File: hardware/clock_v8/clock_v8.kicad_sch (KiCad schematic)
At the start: 143 parts, among them J1 RJ45, J12 Conn_01x06, J2 Conn_01x06_Pin, J4 USB_C_Receptacle, J5 Conn_01x06_Pin, J6 Conn_01x04_Pin, J8 Conn_01x02, Q1 2N7002, Q10 2N7002, Q9 2N7002, U1 ADA4807-1, U10 STM32F405RGTx, U11 AMS1117-3.3, U12 BA50DD0WHFP-TR, U13 M24C02-RMN, U14 CH340C, U15 USBLC6-2P6, U2 SN74LVC1G14DBV, U3 SN74LVC1G14DBV, U4 ADA4807-1, U5 ADA4807-1, U6 TLV3603DCKR, U7 SN74LVC1G14DBV, U8 TLV3603DCKR, U9 L78L05_SOT89, Y1 AOCJY4A-10.000MHZ-SW, Y2 16MHz

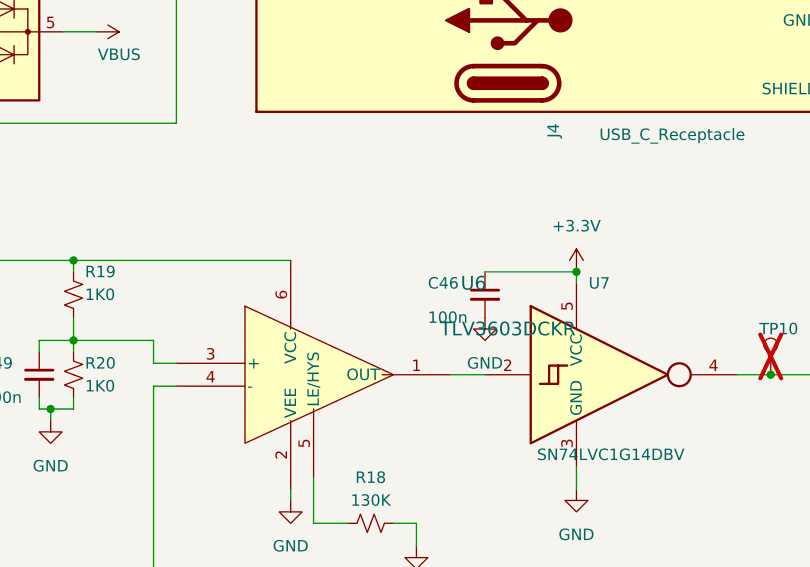
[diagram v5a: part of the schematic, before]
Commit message: move symbols and footprints to shared level
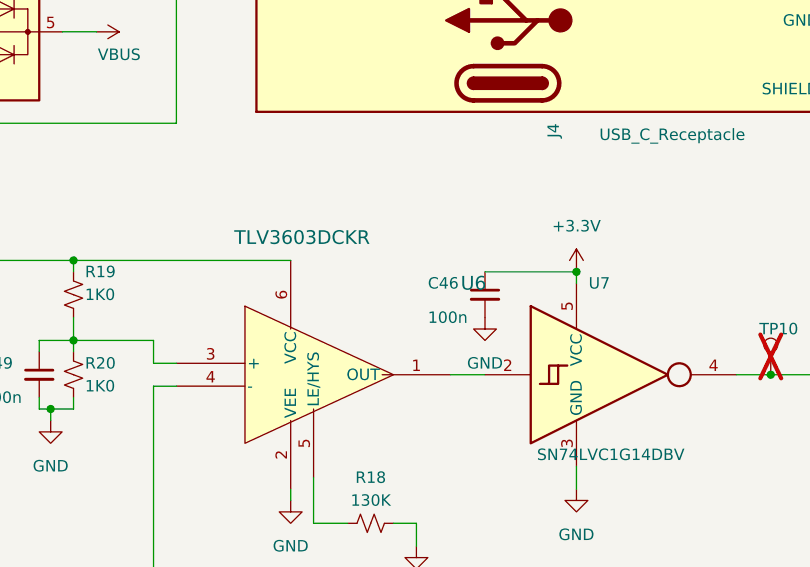
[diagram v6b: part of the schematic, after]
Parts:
- J4: symbol blinky:USB_C_Receptacle -> BlinkyShared:USB_C_Receptacle
- S1, S2, S3: symbol blinky:147873-2 -> BlinkyShared:147873-2
- U12: footprint blinky_footprints:DPAK172P1054X200-6N -> DPAK172P1054X200-6N; symbol blinky:BA50DD0WHFP-TR -> BlinkyShared:BA50DD0WHFP-TR; MAXIMUM_PACKAGE_HEIGHT (none) -> 2.005 mm; PARTREV (none) -> 003; STANDARD (none) -> IPC 7351B
- U6, U8: symbol blinky:TLV3603DCKR -> BlinkyShared:TLV3603DCKR
- Y1: footprint blinky_footprints:XTAL_AOCJY4A-10.000MHZ-SW -> XTAL_AOCJY4A-10.000MHZ-SW; symbol blinky:AOCJY4A-10.000MHZ-SW -> BlinkyShared:AOCJY4A-10.000MHZ-SW; MAXIMUM_PACKAGE_HEIGHT (none) -> 13.76 mm; PARTREV (none) -> 07.24.11; SNAPEDA_PN (none) -> AOCJY4A-10.000MHZ-SW; STANDARD (none) -> IPC_7351B; now in the parts list
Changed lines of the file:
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@@
   (junction (at 391.16 214.63) (diameter 0) (color 0 0 0 0)
   )
-  (junction (at 283.21 237.49) (diameter 0) (color 0 0 0 0)
-  )
   (junction (at 49.53 60.96) (diameter 0) (color 0 0 0 0)
   )
@@
   (junction (at 364.49 214.63) (diameter 0) (color 0 0 0 0)
   )
+  (junction (at 283.21 237.49) (diameter 0) (color 0 0 0 0)
+  )
   (junction (at 20.32 53.34) (diameter 0) (color 0 0 0 0)
   )
@@
     (stroke (width 0) (type default))
   )
-  (wire (pts (xy 283.21 237.49) (xy 283.21 241.3))
-    (stroke (width 0) (type default))
-  )
   (wire (pts (xy 229.87 252.73) (xy 236.22 252.73))
     (stroke (width 0) (type default))
@@
     (stroke (width 0) (type default))
   )
+  (wire (pts (xy 283.21 237.49) (xy 283.21 241.3))
+    (stroke (width 0) (type default))
+  )
   (wire (pts (xy 364.49 138.43) (xy 377.19 138.43))
     (stroke (width 0) (type default))
@@
     )
   )
-  (symbol (lib_id "blinky:AOCJY4A-10.000MHZ-SW") (at 252.73 160.02 0) (unit 1)
-    (in_bom no) (on_board yes) (dnp yes) (fields_autoplaced)
+  (symbol (lib_id "BlinkyShared:AOCJY4A-10.000MHZ-SW") (at 252.73 160.02 0) (unit 1)
+    (in_bom yes) (on_board yes) (dnp yes) (fields_autoplaced)
     (property "Reference" "Y1" (at 252.73 144.78 0)
       (effects (font (size 1.27 1.27)))
@@
       (effects (font (size 1.27 1.27)))
     )
-    (property "Footprint" "blinky_footprints:XTAL_AOCJY4A-10.000MHZ-SW" (at 252.73 160.02 0)
+    (property "Footprint" "XTAL_AOCJY4A-10.000MHZ-SW" (at 252.73 160.02 0)
       (effects (font (size 1.27 1.27)) (justify bottom) hide)
     )
@@
       (effects (font (size 1.27 1.27)) hide)
     )
-    (property "PARTREV" "" (at 252.73 160.02 0)
+    (property "PARTREV" "07.24.11" (at 252.73 160.02 0)
       (effects (font (size 1.27 1.27)) (justify bottom) hide)
     )
-    (property "STANDARD" "" (at 252.73 160.02 0)
+    (property "STANDARD" "IPC_7351B" (at 252.73 160.02 0)
       (effects (font (size 1.27 1.27)) (justify bottom) hide)
     )
-    (property "SNAPEDA_PN" "" (at 252.73 160.02 0)
+    (property "SNAPEDA_PN" "AOCJY4A-10.000MHZ-SW" (at 252.73 160.02 0)
       (effects (font (size 1.27 1.27)) (justify bottom) hide)
     )
-    (property "MAXIMUM_PACKAGE_HEIGHT" "" (at 252.73 160.02 0)
+    (property "MAXIMUM_PACKAGE_HEIGHT" "13.76 mm" (at 252.73 160.02 0)
       (effects (font (size 1.27 1.27)) (justify bottom) hide)
     )
@@
     )
   )
-  (symbol (lib_id "blinky:BA50DD0WHFP-TR") (at 46.99 171.45 0) (unit 1)
+  (symbol (lib_id "BlinkyShared:BA50DD0WHFP-TR") (at 46.99 171.45 0) (unit 1)
     (in_bom yes) (on_board yes) (dnp no) (fields_autoplaced)
     (property "Reference" "U12" (at 46.99 158.75 0)
@@
       (effects (font (size 1.27 1.27)))
     )
-    (property "Footprint" "blinky_footprints:DPAK172P1054X200-6N" (at 46.99 171.45 0)
+    (property "Footprint" "DPAK172P1054X200-6N" (at 46.99 171.45 0)
       (effects (font (size 1.27 1.27)) (justify bottom) hide)
     )
@@
       (effects (font (size 1.27 1.27)) hide)
     )
-    (property "PARTREV" "" (at 46.99 171.45 0)
+    (property "PARTREV" "003" (at 46.99 171.45 0)
       (effects (font (size 1.27 1.27)) (justify bottom) hide)
     )
@@
       (effects (font (size 1.27 1.27)) (justify bottom) hide)
     )
-    (property "MAXIMUM_PACKAGE_HEIGHT" "" (at 46.99 171.45 0)
+    (property "MAXIMUM_PACKAGE_HEIGHT" "2.005 mm" (at 46.99 171.45 0)
       (effects (font (size 1.27 1.27)) (justify bottom) hide)
     )
-    (property "STANDARD" "" (at 46.99 171.45 0)
+    (property "STANDARD" "IPC 7351B" (at 46.99 171.45 0)
       (effects (font (size 1.27 1.27)) (justify bottom) hide)
     )
@@
     )
   )
-  (symbol (lib_id "blinky:TLV3603DCKR") (at 265.43 237.49 0) (unit 1)
+  (symbol (lib_id "BlinkyShared:TLV3603DCKR") (at 265.43 237.49 0) (unit 1)
     (in_bom yes) (on_board yes) (dnp no)
     (property "Reference" "U8" (at 273.05 232.41 0)
@@
     )
   )
-  (symbol (lib_id "blinky:147873-2") (at 40.64 111.76 0) (unit 1)
+  (symbol (lib_id "BlinkyShared:147873-2") (at 40.64 111.76 0) (unit 1)
     (in_bom yes) (on_board yes) (dnp no) (fields_autoplaced)
     (property "Reference" "S3" (at 40.64 105.41 0)
@@
     )
   )
-  (symbol (lib_id "blinky:USB_C_Receptacle") (at 377.19 46.99 90) (unit 1)
+  (symbol (lib_id "BlinkyShared:USB_C_Receptacle") (at 377.19 46.99 90) (unit 1)
     (in_bom yes) (on_board yes) (dnp no)
     (property "Reference" "J4" (at 382.27 58.42 0)
@@
       (effects (font (size 1.27 1.27)) hide)
     )
+    (property "JLCPCB#" "" (at 377.19 46.99 0)
+      (effects (font (size 1.27 1.27)) hide)
+    )
     (pin "A1")
     (pin "A12")
@@
     )
   )
-  (symbol (lib_name "TLV3603DCKR_1") (lib_id "blinky:TLV3603DCKR") (at 353.06 86.36 0) (unit 1)
+  (symbol (lib_id "BlinkyShared:TLV3603DCKR") (at 353.06 86.36 0) (unit 1)
     (in_bom yes) (on_board yes) (dnp no)
     (property "Reference" "U6" (at 373.38 76.2 0)
       (effects (font (size 1.524 1.524)))
     )
-    (property "Value" "TLV3603DCKR" (at 377.19 81.28 0)
+    (property "Value" "TLV3603DCKR" (at 354.33 71.12 0)
       (effects (font (size 1.524 1.524)))
     )
@@
     )
   )
-  (symbol (lib_id "blinky:147873-2") (at 35.56 139.7 0) (unit 1)
+  (symbol (lib_id "BlinkyShared:147873-2") (at 35.56 139.7 0) (unit 1)
     (in_bom yes) (on_board yes) (dnp no) (fields_autoplaced)
     (property "Reference" "S2" (at 35.56 133.35 0)
@@
     )
   )
-  (symbol (lib_id "blinky:147873-2") (at 35.56 124.46 0) (unit 1)
+  (symbol (lib_id "BlinkyShared:147873-2") (at 35.56 124.46 0) (unit 1)
     (in_bom yes) (on_board yes) (dnp no) (fields_autoplaced)
     (property "Reference" "S1" (at 35.56 118.11 0)

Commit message: clean up clock
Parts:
- removed TP19: ~, TestPoint:TestPoint_THTPad_D1.5mm_Drill0.7mm, symbol Connector:TestPoint
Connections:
- no-connect marks 34 -> 36
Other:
- moved on the sheet: C18, C24, C26, R12, R13, R14, R15, R16, R17, R23, R24, R8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

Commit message: starting 10Mhz Aux clk input
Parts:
- removed S2: 147873-2, SW_147873-2, symbol BlinkyShared:147873-2
- added C51, C52, C53: 100n, Capacitor_SMD:C_0402_1005Metric, symbol Device:C_Small
- added C54: 100n, Capacitor_SMD:C_0603_1608Metric, symbol Device:C_Small
- added J?: KH-BNC50-3511, blinky_footprints:BNC_Amphenol_B6252HB-NPP3G-50_Horizontal-CJ, symbol Connector:Conn_Coaxial
- added JP1, JP2: SolderJumper_2_Bridged, Jumper:SolderJumper-2_P1.3mm_Bridged2Bar_RoundedPad1.0x1.5mm, symbol Jumper:SolderJumper_2_Bridged
- added Q2: S8550, Package_TO_SOT_SMD:SC-59, symbol Transistor_BJT:S8550
- added Q3: S8050, Package_TO_SOT_SMD:SC-59, symbol Transistor_BJT:S8050
- added R39: 200R, Resistor_SMD:R_0805_2012Metric, symbol Device:R_Small_US
- added R40: 4K7, Resistor_SMD:R_0603_1608Metric, symbol Device:R_US
- added R41, R42, R43, R44: 1K0, Resistor_SMD:R_0603_1608Metric, symbol Device:R_Small_US
- added R45: 130K, Resistor_SMD:R_0603_1608Metric, symbol Device:R_Small_US
- added R46, R47: 100R, Resistor_SMD:R_0603_1608Metric, symbol Device:R_Small_US
- added SW1: LC1258OASP, blinky_footprints:LC1258OASP, symbol BlinkyShared:LC1258OASP
- added TP1: ~, TestPoint:TestPoint_THTPad_D1.5mm_Drill0.7mm, symbol Connector:TestPoint
- added U16: TLV3603DCKR, SC70_DCK_TEX, symbol BlinkyShared:TLV3603DCKR
- added U17: SN74LVC1G14DBV, Package_TO_SOT_SMD:SOT-23-5, symbol 74xGxx:SN74LVC1G14DBV
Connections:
- net +3.3V: now also C53.1, Q2.1 (E), SW1.2, U17.5 (VCC)
- net +5VA: now also C52.1, R43.1, R46.1, U16.6 (VCC)
- net AUX_CLK: now also TP1.1, U17.4
- net BOOT0: now also JP2.1 (A)
- net BTN1: now also R39.2, R40.2
- net GND: now also C51.2, C52.2, C53.2, J?.2 (Ext), Q3.1 (E), R40.1, R44.2, R45.2, R47.2, SW1.4, SW1.5, U16.2 (VEE), U17.3 (GND)
- net NRST: now also JP1.1 (A)
- net USB_DTR: now also R41.2
- net USB_RTS: now also R42.2
- new net: C54.2, R46.2, R47.1, U16.4 (-)
- new net: C51.1, R43.2, R44.1, U16.3 (+)
- new net: U16.1 (OUT), U17.2
- new net: R45.1, U16.5 (LE/HYS)
- new net: JP2.2 (B), Q2.3 (C)
- new net: Q3.2 (B), R42.1
- new net: Q2.2 (B), R41.1
- new net: R39.1, SW1.1
- new net: JP1.2 (B), Q3.3 (C)
- new net: C54.1, J?.1 (In)
- no-connect marks 36 -> 35
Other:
- moved on the sheet: C17, C19, C2, C20, C21, C22, C23, C24, C3, C46, C47, C49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
